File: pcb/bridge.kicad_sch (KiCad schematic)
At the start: 15 parts, among them Q1 IRFR7540TRPBF, Q2 IRFR7540TRPBF, Q3 IRFR7540TRPBF, Q4 IRFR7540TRPBF, Q5 IRFR7540TRPBF, Q6 IRFR7540TRPBF

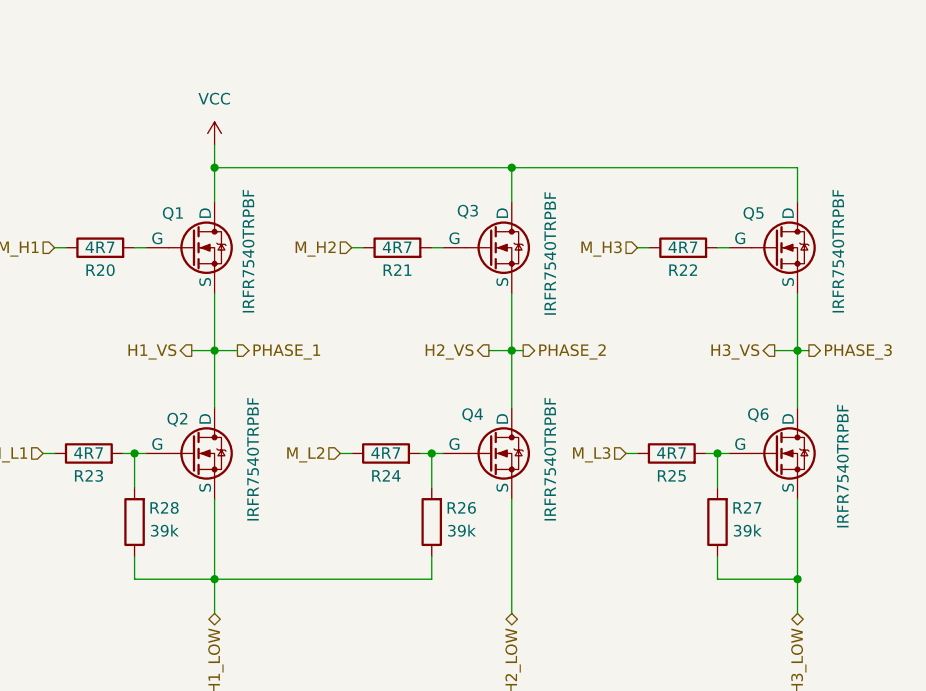
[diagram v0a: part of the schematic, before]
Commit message: pcb: outlines ready
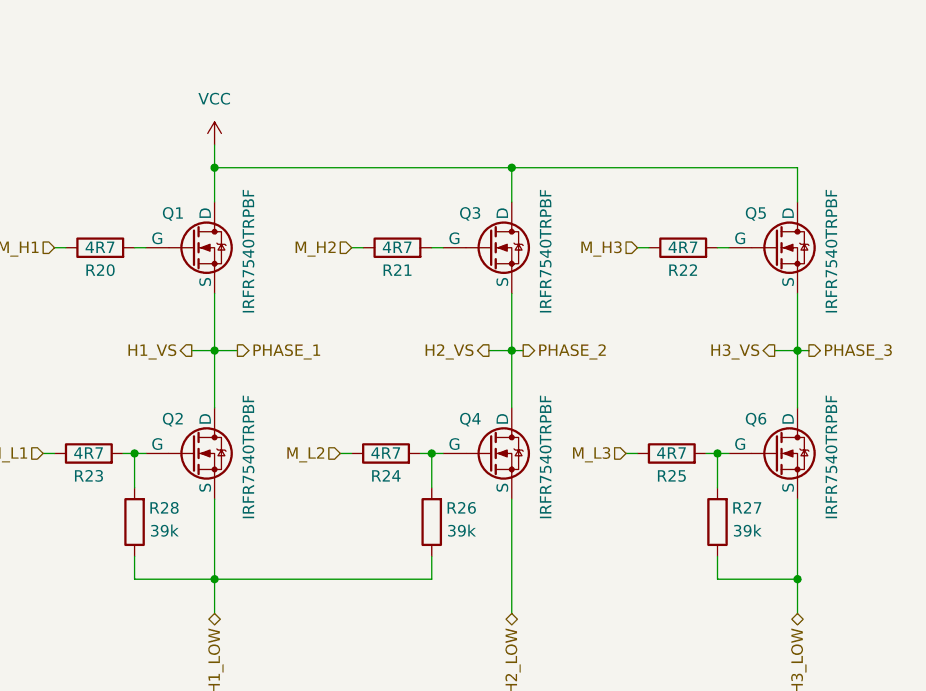
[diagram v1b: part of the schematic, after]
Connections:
- net H1_VS: now also Q2.2 (D); no longer Q2.1 (D)
- net H2_VS: now also Q4.2 (D); no longer Q4.1 (D)
- net H3_VS: now also Q6.2 (D); no longer Q6.1 (D)
- net VCC: now also Q1.2 (D), Q3.2 (D), Q5.2 (D); no longer Q1.1 (D), Q3.1 (D), Q5.1 (D)
- net at R20.2: now also Q1.1 (G); no longer Q1.2 (G)
- net at R24.2, R26.2: now also Q4.1 (G); no longer Q4.2 (G)
- net at R23.2, R28.2: now also Q2.1 (G); no longer Q2.2 (G)
- net at R22.2: now also Q5.1 (G); no longer Q5.2 (G)
- net at R21.2: now also Q3.1 (G); no longer Q3.2 (G)
- net at R25.2, R27.2: now also Q6.1 (G); no longer Q6.2 (G)
